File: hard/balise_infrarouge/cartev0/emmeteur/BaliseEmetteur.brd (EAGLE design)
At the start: 76.2 x 76.2 mm, 65 parts, among them IC1 MEGA8-AI, IC2 74AHC1G02DBV, IC3 7812TV, Q1 16MHz, T1 2SC1307

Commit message: maj emetteur + fini recepteur part 1
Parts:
- moved C7 2.39 mm to (36.6, 28.2)
- renumbered JP2 to FTDI_ARDUINO
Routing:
- net GND: track 107.8 -> 109.8 mm
- net N$8: track 15.1 -> 13.2 mm
- net +5V: vias 3 -> 2

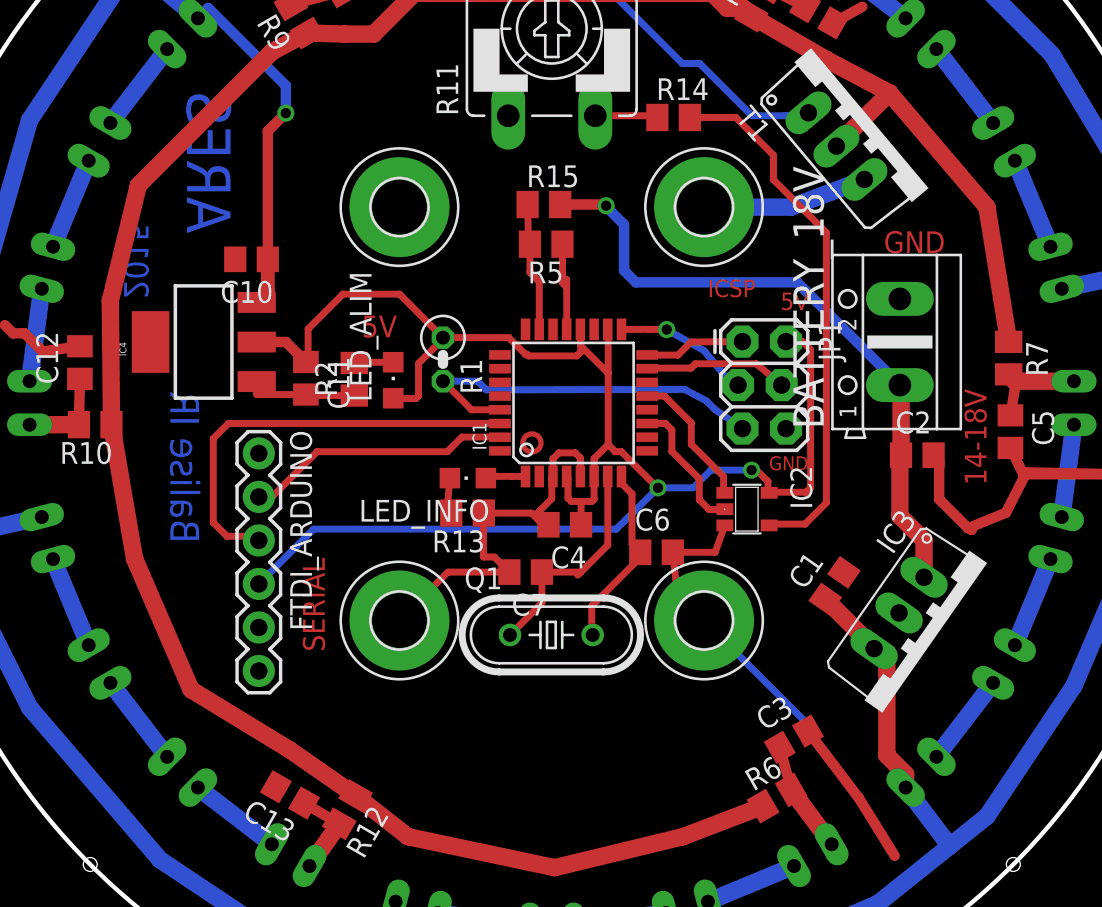
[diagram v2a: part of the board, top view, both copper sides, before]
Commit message: maj connectyeur bt + ftdi carte elettrice
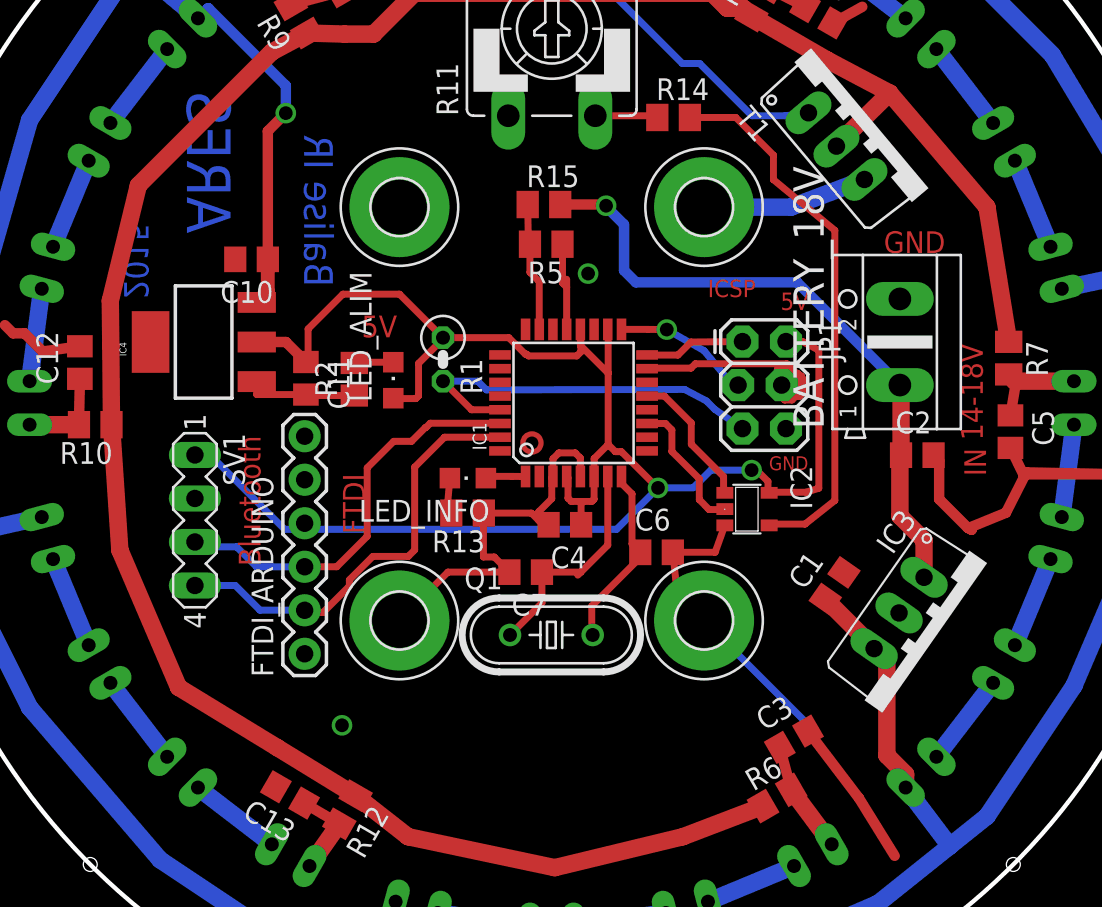
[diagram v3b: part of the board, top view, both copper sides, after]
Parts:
- added SV1: Bluetooth, con-lstb:MA04-1
- moved FTDI_ARDUINO 12.0 mm to (23.7, 23.5), turned to 90 degrees
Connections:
- net +5V: now also SV1.1
- net GND: now also SV1.2
- net UART_RX: now also SV1.3
- net UART_TX: now also SV1.4
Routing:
- net ISP_MOSI: track 8.43 -> 19.7 mm
- net UART_TX: track 15.5 -> 25.7 mm
- net +5V: track 98.3 -> 103.9 mm
- net UART_RX: track 25.1 -> 24.2 mm
- net N$3: track 31.2 -> 32.0 mm
- net GND: vias 0 -> 2
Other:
- board text added: "Bluetooth"
- board text added: "FTDI"
- board text added: "IN"
- board text removed: "SERIAL"
